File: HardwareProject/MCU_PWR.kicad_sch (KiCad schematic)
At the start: 29 parts, among them U4 HPM6P41IPB1

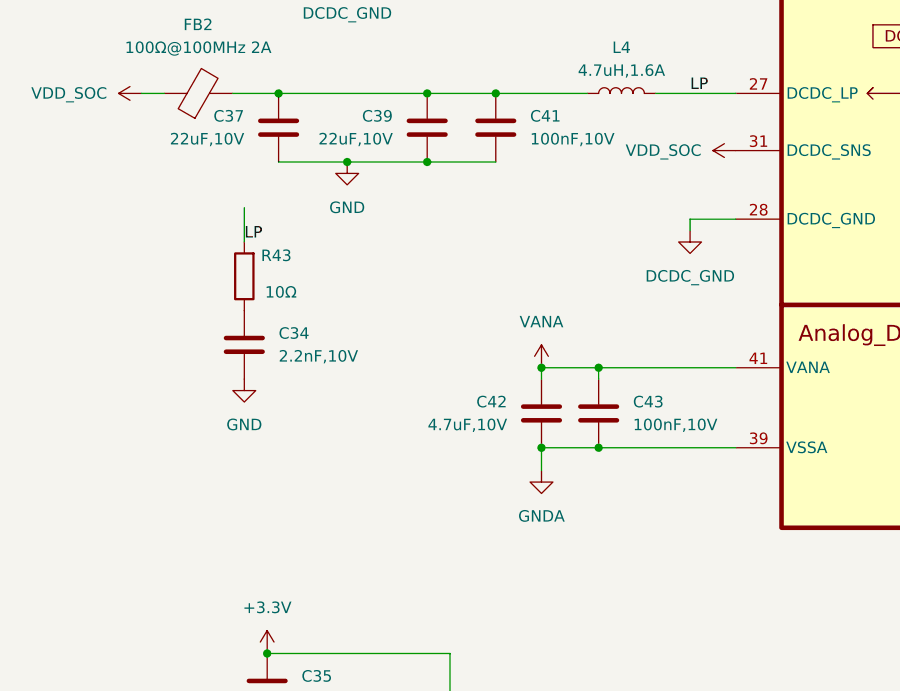
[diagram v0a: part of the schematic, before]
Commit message: 修改了UCC27211A封装，此芯片此前的封装均错误 修改了采样线布局，为SAR ADC加入前置RC
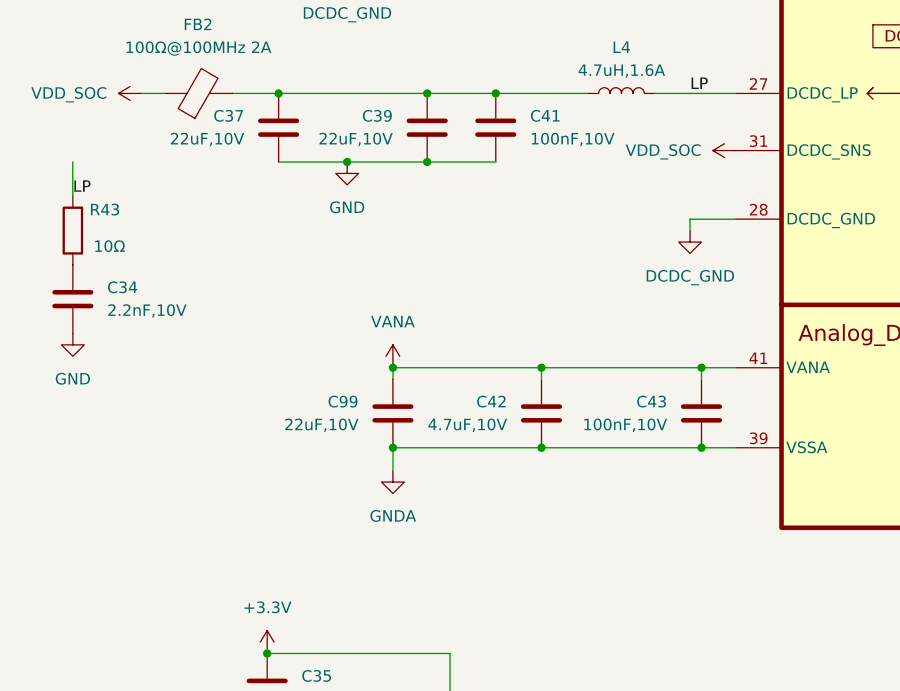
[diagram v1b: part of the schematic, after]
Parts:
- added C99: 22uF,10V, Capacitor_SMD:C_0603_1608Metric, symbol Device:C
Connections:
- net GNDA: now also C99.2
- net VANA: now also C99.1
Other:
- moved on the sheet: C34, C43, R43
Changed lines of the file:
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@@
 	)
 	(junction
-		(at 105.41 95.25)
+		(at 93.98 34.29)
 		(diameter 0)
 		(color 0 0 0 0)
 	)
 	(junction
-		(at 93.98 34.29)
+		(at 82.55 95.25)
 		(diameter 0)
 		(color 0 0 0 0)
@@
 	)
 	(junction
+		(at 82.55 86.36)
+		(diameter 0)
+		(color 0 0 0 0)
+	)
+	(junction
 		(at 175.26 52.07)
 		(diameter 0)
@@
 	)
 	(junction
+		(at 116.84 95.25)
+		(diameter 0)
+		(color 0 0 0 0)
+	)
+	(junction
 		(at 86.36 63.5)
 		(diameter 0)
@@
 	)
 	(junction
-		(at 105.41 86.36)
-		(diameter 0)
-		(color 0 0 0 0)
-	)
-	(junction
 		(at 177.8 86.36)
 		(diameter 0)
@@
 	)
 	(junction
+		(at 116.84 86.36)
+		(diameter 0)
+		(color 0 0 0 0)
+	)
+	(junction
 		(at 196.85 52.07)
 		(diameter 0)
@@
 	(wire
 		(pts
-			(xy 66.04 68.58) (xy 66.04 72.39)
+			(xy 116.84 95.25) (xy 120.65 95.25)
+		)
+		(stroke
+			(width 0)
+			(type default)
+		)
+	)
+	(wire
+		(pts
+			(xy 46.99 63.5) (xy 46.99 67.31)
 		)
 		(stroke
@@
 	(wire
 		(pts
-			(xy 105.41 95.25) (xy 120.65 95.25)
+			(xy 116.84 86.36) (xy 120.65 86.36)
 		)
 		(stroke
@@
 	(wire
 		(pts
-			(xy 240.03 133.35) (xy 246.38 133.35)
+			(xy 82.55 86.36) (xy 99.06 86.36)
 		)
 		(stroke
@@
 	(wire
 		(pts
-			(xy 105.41 86.36) (xy 120.65 86.36)
+			(xy 240.03 133.35) (xy 246.38 133.35)
 		)
 		(stroke
@@
 	(wire
 		(pts
-			(xy 99.06 86.36) (xy 105.41 86.36)
+			(xy 99.06 86.36) (xy 116.84 86.36)
 		)
 		(stroke
@@
 	(wire
 		(pts
-			(xy 99.06 95.25) (xy 105.41 95.25)
+			(xy 99.06 95.25) (xy 116.84 95.25)
 		)
 		(stroke
@@
 	(wire
 		(pts
-			(xy 105.41 86.36) (xy 105.41 87.63)
+			(xy 116.84 86.36) (xy 116.84 87.63)
 		)
 		(stroke
@@
 		)
 	)
+	(wire
+		(pts
+			(xy 82.55 95.25) (xy 82.55 97.79)
+		)
+		(stroke
+			(width 0)
+			(type default)
+		)
+	)
 	(bus
 		(pts
@@
 	(wire
 		(pts
-			(xy 99.06 95.25) (xy 99.06 97.79)
+			(xy 82.55 86.36) (xy 82.55 87.63)
 		)
 		(stroke
@@
 		)
 	)
+	(wire
+		(pts
+			(xy 82.55 95.25) (xy 99.06 95.25)
+		)
+		(stroke
+			(width 0)
+			(type default)
+		)
+	)
 	(label "LP"
-		(at 66.04 72.39 0)
+		(at 46.99 67.31 0)
 		(effects
 			(font
@@
 	(symbol
 		(lib_id "power:+5V")
-		(at 99.06 86.36 0)
+		(at 82.55 86.36 0)
 		(unit 1)
 		(exclude_from_sim no)
@@
 		(fields_autoplaced yes)
 		(property "Reference" "#PWR088"
-			(at 99.06 90.17 0)
+			(at 82.55 90.17 0)
 			(effects
 				(font
@@
 		)
 		(property "Value" "VANA"
-			(at 99.06 81.28 0)
+			(at 82.55 81.28 0)
 			(effects
 				(font
@@
 		)
 		(property "Footprint" ""
-			(at 99.06 86.36 0)
+			(at 82.55 86.36 0)
 			(effects
 				(font
@@
 		)
 		(property "Datasheet" ""
-			(at 99.06 86.36 0)
+			(at 82.55 86.36 0)
 			(effects
 				(font
@@
 		)
 		(property "Description" "Power symbol creates a global label with name \"+5V\""
-			(at 99.06 86.36 0)
+			(at 82.55 86.36 0)
 			(effects
 				(font
@@
 	(symbol
 		(lib_id "Device:C")
-		(at 66.04 83.82 0)
+		(at 46.99 78.74 0)
 		(unit 1)
 		(exclude_from_sim no)
@@
 		(dnp no)
 		(property "Reference" "C34"
-			(at 69.85 82.5499 0)
+			(at 50.8 77.4699 0)
 			(effects
 				(font
@@
 		)
 		(property "Value" "2.2nF,10V"
-			(at 69.85 85.0899 0)
+			(at 50.8 80.0099 0)
 			(effects
 				(font
@@
 		)
 		(property "Footprint" "Capacitor_SMD:C_0603_1608Metric"
-			(at 67.0052 87.63 0)
+			(at 47.9552 82.55 0)
 			(effects
 				(font
@@
 		)
 		(property "Datasheet" "~"
-			(at 66.04 83.82 0)
+			(at 46.99 78.74 0)
 			(effects
 				(font
@@
 		)
 		(property "Description" "Unpolarized capacitor"
-			(at 66.04 83.82 0)
+			(at 46.99 78.74 0)
 			(effects
 				(font
@@
 	(symbol
 		(lib_id "Device:C")
+		(at 82.55 91.44 0)
+		(mirror y)
+		(unit 1)
+		(exclude_from_sim no)
+		(in_bom yes)
+		(on_board yes)
+		(dnp no)
+		(property "Reference" "C99"
+			(at 78.74 90.1699 0)
+			(effects
+				(font
+					(size 1.27 1.27)
+				)
+				(justify left)
+			)
+		)
+		(property "Value" "22uF,10V"
+			(at 78.74 92.7099 0)
+			(effects
+				(font
+					(size 1.27 1.27)
+				)
+				(justify left)
+			)
+		)
+		(property "Footprint" "Capacitor_SMD:C_0603_1608Metric"
+			(at 81.5848 95.25 0)
+			(effects
+				(font
+					(size 1.27 1.27)
+				)
+				(hide yes)
+			)
+		)
+		(property "Datasheet" "~"
+			(at 82.55 91.44 0)
+			(effects
+				(font
+					(size 1.27 1.27)
+				)
+				(hide yes)
+			)
+		)
+		(property "Description" "Unpolarized capacitor"
+			(at 82.55 91.44 0)
+			(effects
+				(font
+					(size 1.27 1.27)
+				)
+				(hide yes)
+			)
+		)
+		(pin "1"
+		)
+		(pin "2"
+		)
+		(instances
+			(project "HPM6P41_BB"
+				(path "/714b8a30-f9a7-49d4-a000-bc20c4884c7a/dfb16f69-5c04-494c-819f-f5ce473aeb21"
+					(reference "C99")
+					(unit 1)
+				)
+			)
+		)
+	)
+	(symbol
+		(lib_id "Device:C")
 		(at 175.26 55.88 0)
 		(unit 1)
@@
 	(symbol
 		(lib_id "Device:R")
-		(at 66.04 76.2 180)
+		(at 46.99 71.12 180)
 		(unit 1)
 		(exclude_from_sim no)
@@
 		(dnp no)
 		(property "Reference" "R43"
-			(at 69.596 73.914 0)
+			(at 50.546 68.834 0)
 			(effects
 				(font
@@
 		)
 		(property "Value" "10Ω"
-			(at 70.104 77.978 0)
+			(at 51.054 72.898 0)
 			(effects
 				(font
@@
 		)
 		(property "Footprint" "Resistor_SMD:R_0603_1608Metric"
-			(at 67.818 76.2 90)
+			(at 48.768 71.12 90)
 			(effects
 				(font
@@
 		)
 		(property "Datasheet" "~"
-			(at 66.04 76.2 0)
+			(at 46.99 71.12 0)
 			(effects
 				(font
@@
 		)
 		(property "Description" "Resistor"
-			(at 66.04 76.2 0)
+			(at 46.99 71.12 0)
 			(effects
 				(font
@@
 	(symbol
 		(lib_id "Device:C")
-		(at 105.41 91.44 0)
+		(at 116.84 91.44 0)
+		(mirror y)
 		(unit 1)
 		(exclude_from_sim no)
@@
 		(dnp no)
 		(property "Reference" "C43"
-			(at 109.22 90.1699 0)
+			(at 113.03 90.1699 0)
 			(effects
 				(font
@@
 		)
 		(property "Value" "100nF,10V"
-			(at 109.22 92.7099 0)
+			(at 113.03 92.7099 0)
 			(effects
 				(font
@@
 		)
 		(property "Footprint" "Capacitor_SMD:C_0603_1608Metric"
-			(at 106.3752 95.25 0)
+			(at 115.8748 95.25 0)
 			(effects
 				(font
@@
 		)
 		(property "Datasheet" "~"
-			(at 105.41 91.44 0)
+			(at 116.84 91.44 0)
 			(effects
 				(font
@@
 		)
 		(property "Description" "Unpolarized capacitor"
-			(at 105.41 91.44 0)
+			(at 116.84 91.44 0)
 			(effects
 				(font
@@
 	(symbol
 		(lib_id "power:GND")
-		(at 99.06 97.79 0)
+		(at 82.55 97.79 0)
 		(unit 1)
 		(exclude_from_sim no)
@@
 		(fields_autoplaced yes)
 		(property "Reference" "#PWR089"
-			(at 99.06 104.14 0)
+			(at 82.55 104.14 0)
 			(effects
 				(font
@@
 		)
 		(property "Value" "GNDA"
-			(at 99.06 102.87 0)
+			(at 82.55 102.87 0)
 			(effects
 				(font
@@
 		)
 		(property "Footprint" ""
-			(at 99.06 97.79 0)
+			(at 82.55 97.79 0)
 			(effects
 				(font
@@
 		)
 		(property "Datasheet" ""
-			(at 99.06 97.79 0)
+			(at 82.55 97.79 0)
 			(effects
 				(font
@@
 		)
 		(property "Description" "Power symbol creates a global label with name \"GND\" , ground"
-			(at 99.06 97.79 0)
+			(at 82.55 97.79 0)
 			(effects
 				(font
@@
 	(symbol
 		(lib_id "power:GND")
-		(at 66.04 87.63 0)
+		(at 46.99 82.55 0)
 		(unit 1)
 		(exclude_from_sim no)
@@
 		(fields_autoplaced yes)
 		(property "Reference" "#PWR083"
-			(at 66.04 93.98 0)
+			(at 46.99 88.9 0)
 			(effects
 				(font
@@
 		)
 		(property "Value" "GND"
-			(at 66.04 92.71 0)
+			(at 46.99 87.63 0)
 			(effects
 				(font
@@
 		)
 		(property "Footprint" ""
-			(at 66.04 87.63 0)
+			(at 46.99 82.55 0)
 			(effects
 				(font
@@
 		)
 		(property "Datasheet" ""
-			(at 66.04 87.63 0)
+			(at 46.99 82.55 0)
 			(effects
 				(font
@@
 		)
 		(property "Description" "Power symbol creates a global label with name \"GND\" , ground"
-			(at 66.04 87.63 0)
+			(at 46.99 82.55 0)
 			(effects
 				(font

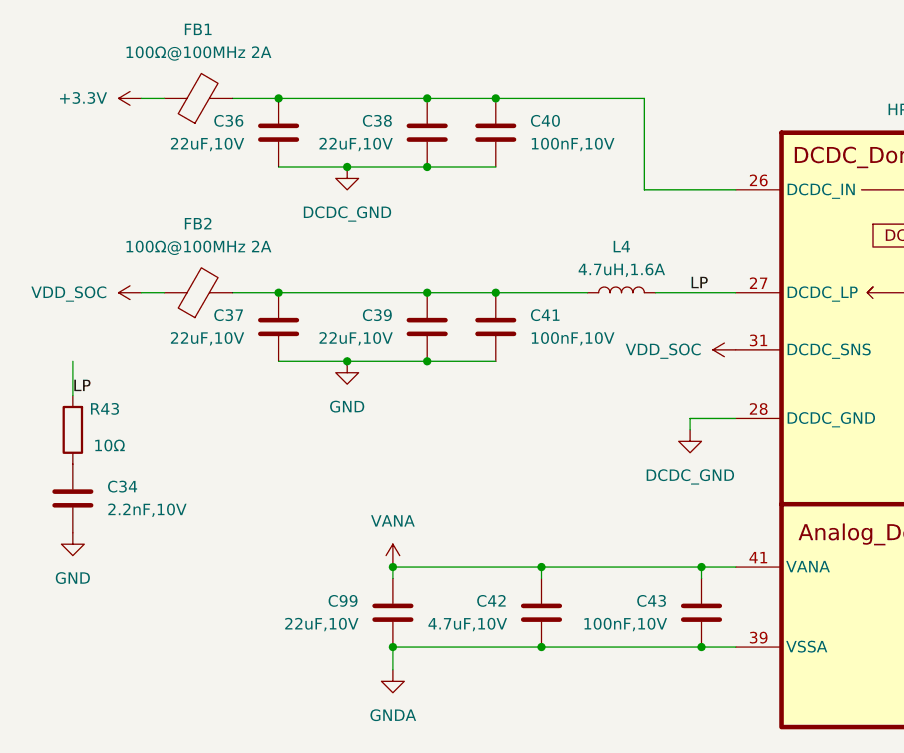
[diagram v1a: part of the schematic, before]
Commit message: 外置核心电压SYR838以改善ADC噪声
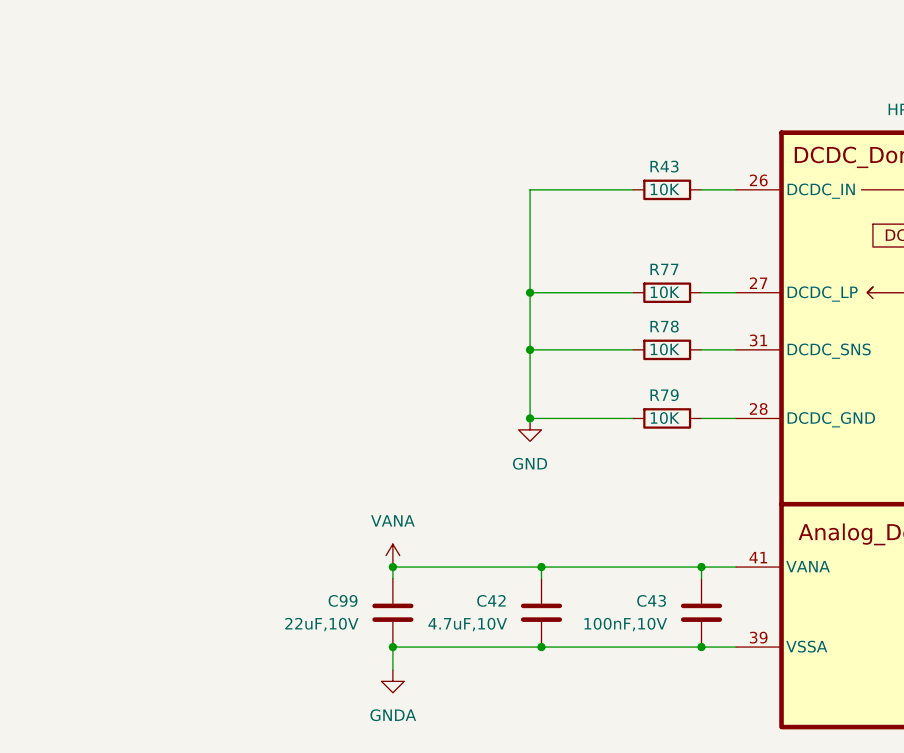
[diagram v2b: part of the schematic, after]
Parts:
- removed C34: 2.2nF,10V, Capacitor_SMD:C_0603_1608Metric, symbol Device:C
- removed C36, C37, C38, C39: 22uF,10V, Capacitor_SMD:C_0603_1608Metric, symbol Device:C
- removed C40, C41: 100nF,10V, Capacitor_SMD:C_0603_1608Metric, symbol Device:C
- removed FB1, FB2: 100Ω@100MHz 2A, Inductor_SMD:L_0603_1608Metric, symbol Device:FerriteBead
- removed L4: 4.7uH,1.6A, Inductor_SMD:L_1210_3225Metric, symbol Device:L
- removed R43: 10Ω, Resistor_SMD:R_0603_1608Metric, symbol Device:R
- added R43, R77, R78, R79: 10K, Resistor_SMD:R_0603_1608Metric, symbol 02_HPM_Resistor:10K_0402
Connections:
- net GND: now also R43.2, R77.2, R78.2, R79.2
- net VDD_SOC: no longer U4.31 (DCDC_SNS)
- net at U4.26 (DCDC_IN): now also R43.1
- net DCDC_GND: no longer names the net of U4.28 (DCDC_GND)
- net DCDC_GND: now also R79.1
- net LP: no longer names the net of U4.27 (DCDC_LP)
- net LP: now also R77.1
- new net: R78.1, U4.31 (DCDC_SNS)

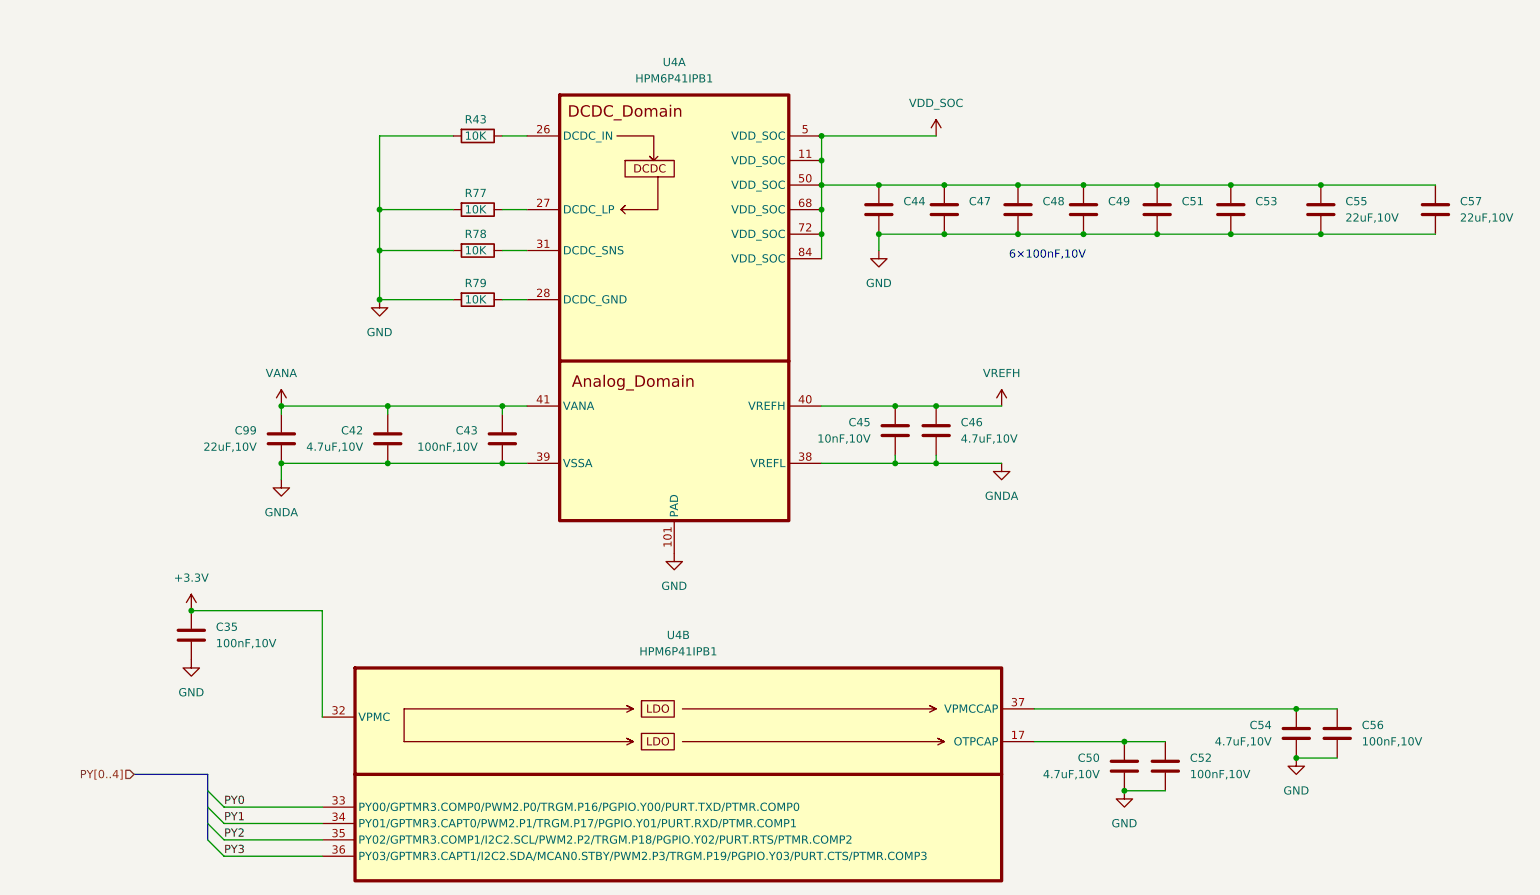
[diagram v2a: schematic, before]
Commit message: rev4修改核心供电前保存（当前SYR838）
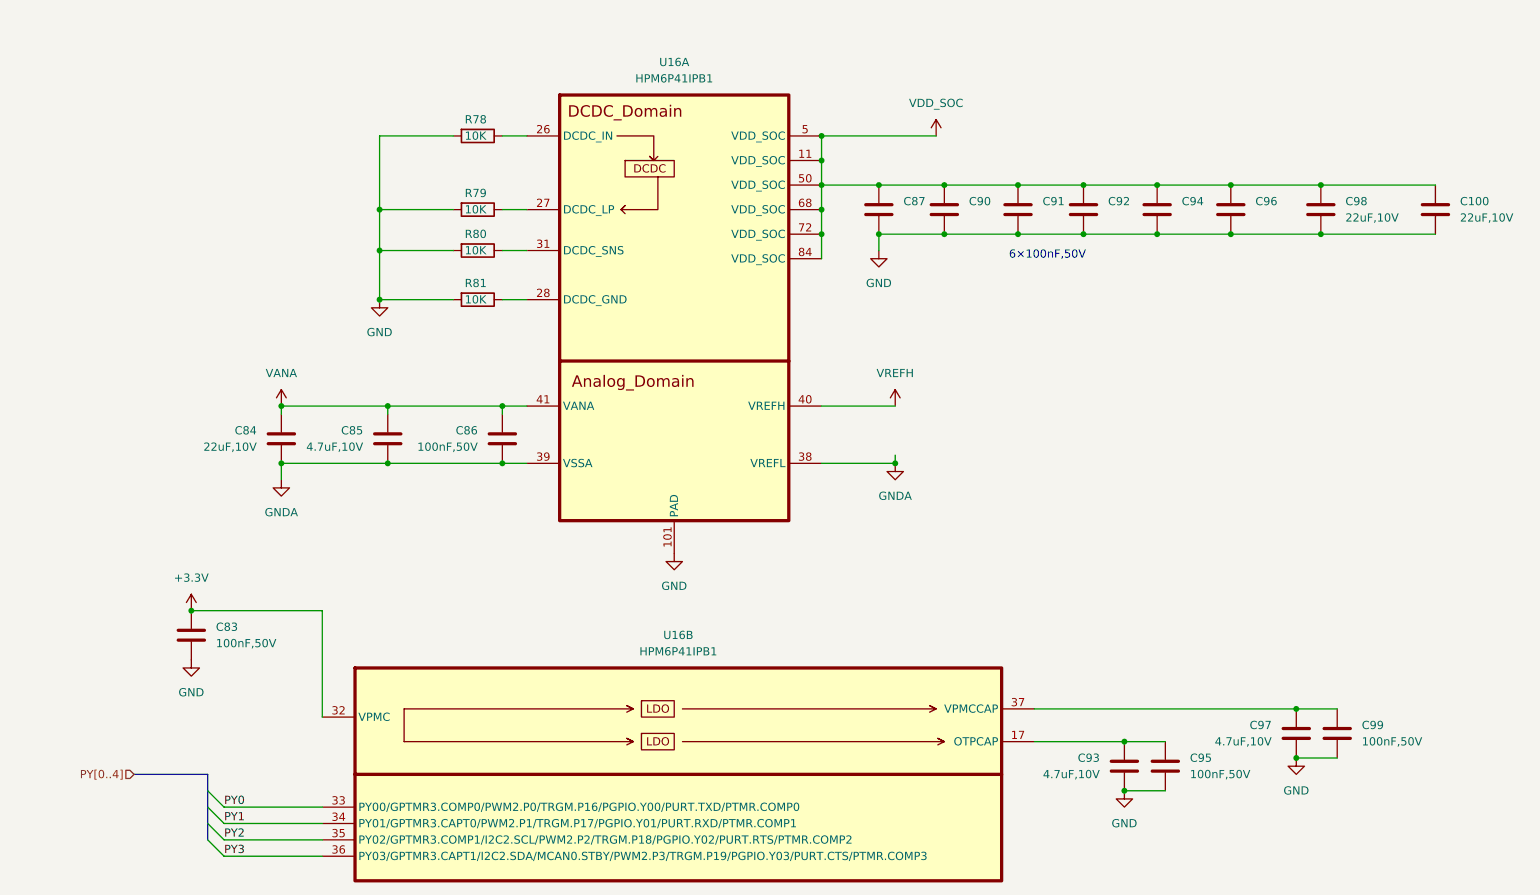
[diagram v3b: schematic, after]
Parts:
- removed C45: 10nF,10V, Capacitor_SMD:C_0603_1608Metric, symbol Device:C
- removed C46: 4.7uF,10V, Capacitor_SMD:C_0603_1608Metric, symbol Device:C
- C83: renamed from C35; value 100nF,10V -> 100nF,50V
- C86: renamed from C43; value 100nF,10V -> 100nF,50V
- C95: renamed from C52; value 100nF,10V -> 100nF,50V
- C99: renamed from C56; value 100nF,10V -> 100nF,50V
- renumbered C57 to C100, C99 to C84, C42 to C85, C44 to C87, C47 to C90, C48 to C91, C49 to C92, C50 to C93, C51 to C94, C53 to C96, C54 to C97, C55 to C98, R43 to R78, R77 to R79, R78 to R80, R79 to R81, U4 to U16
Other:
- note added: "6×100nF,50V"
- note removed: "6×100nF,10V"
